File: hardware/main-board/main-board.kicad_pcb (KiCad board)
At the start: 2 copper layers, 180 x 55 mm, 95 parts, among them J1 BARREL_JACK, J2 CONN_01X10, J3 CONN_01X10, J4 USB_OTG, J5 CONN_02X05, J6 SMA, Q1 DDTD113ZC, Q2 DDTD113ZC, Q3 DDTD113ZC, Q4 DDTD113ZC, Q5 DDTD113ZC, Q6 FDB14N30TM, Q7 DDTD113ZC, Q8 DDTD113ZC, Q9 DDTD113ZC, SW1 SW_Push, SW2 SW_Push, SW3 SW_Push, SW4 SW_Push, U1 LD1117S33TR, U2 MAX1771, U3 STM32F302C, U4 FGPMMOPA6H, Y1 8MHz, Y2 32.768kHz

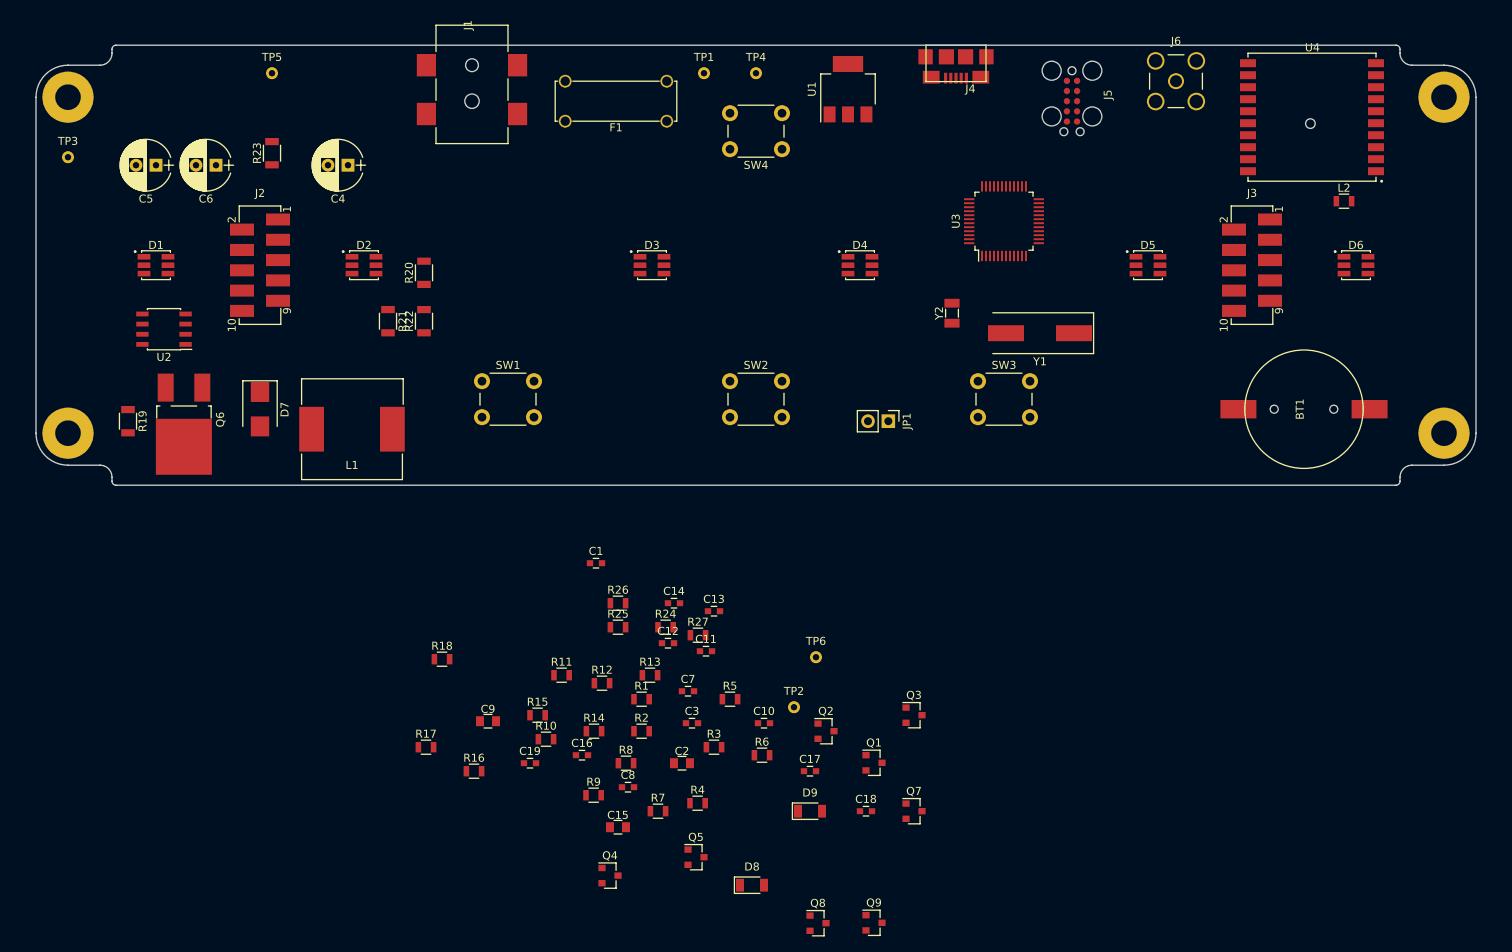
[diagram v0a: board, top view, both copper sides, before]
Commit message: Working on main board layout
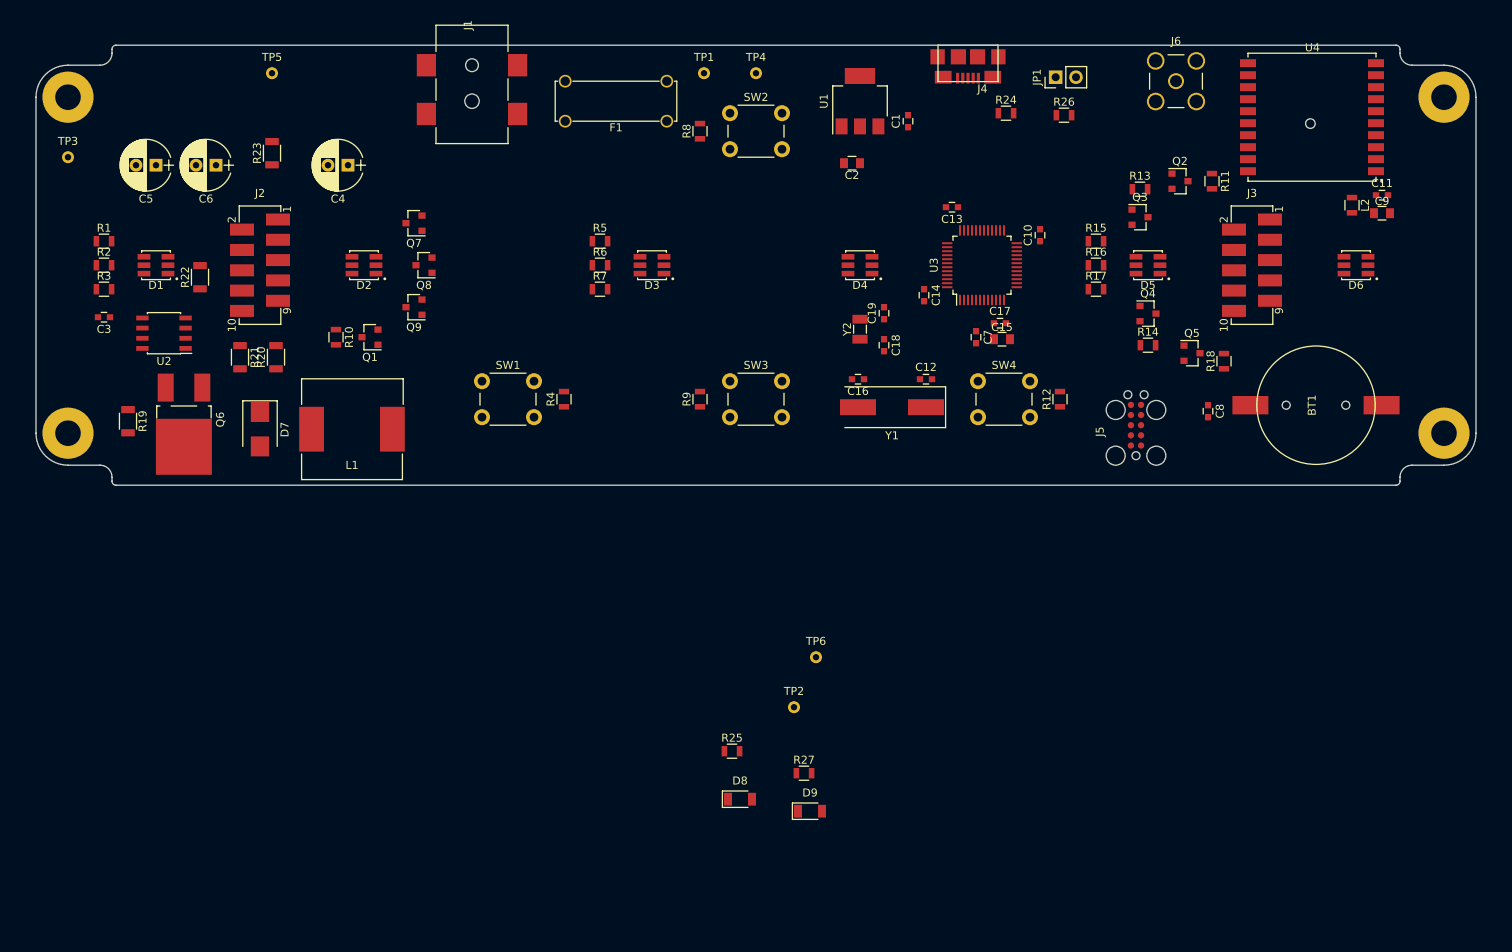
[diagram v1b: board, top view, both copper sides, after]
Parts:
- moved C9 128.5 mm to (228.2, 83.5)
- moved R18 104.6 mm to (208.5, 102.0), turned to 90 degrees
- moved R11 102.1 mm to (207.0, 79.5), turned to 270 degrees
- moved C11 101.9 mm to (228.2, 81.2)
- moved R17 101.4 mm to (192.5, 93.0)
- moved R16 100.2 mm to (192.5, 90.0)
- moved Q4 97.3 mm to (199.0, 96.0)
- moved Q7 96.5 mm to (107.2, 84.8), turned to 180 degrees
- moved Q9 96.1 mm to (107.2, 95.2), turned to 180 degrees
- moved Q8 95.9 mm to (108.5, 90.0), turned to 180 degrees
- moved R3 95.4 mm to (68.5, 93.0)
- moved R15 91.6 mm to (192.5, 87.0)
- moved C3 89.3 mm to (68.5, 96.5), turned to 180 degrees
- moved R2 88.9 mm to (68.5, 90.0)
- moved Q5 88.4 mm to (204.5, 101.0)
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
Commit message: Working on main board layout
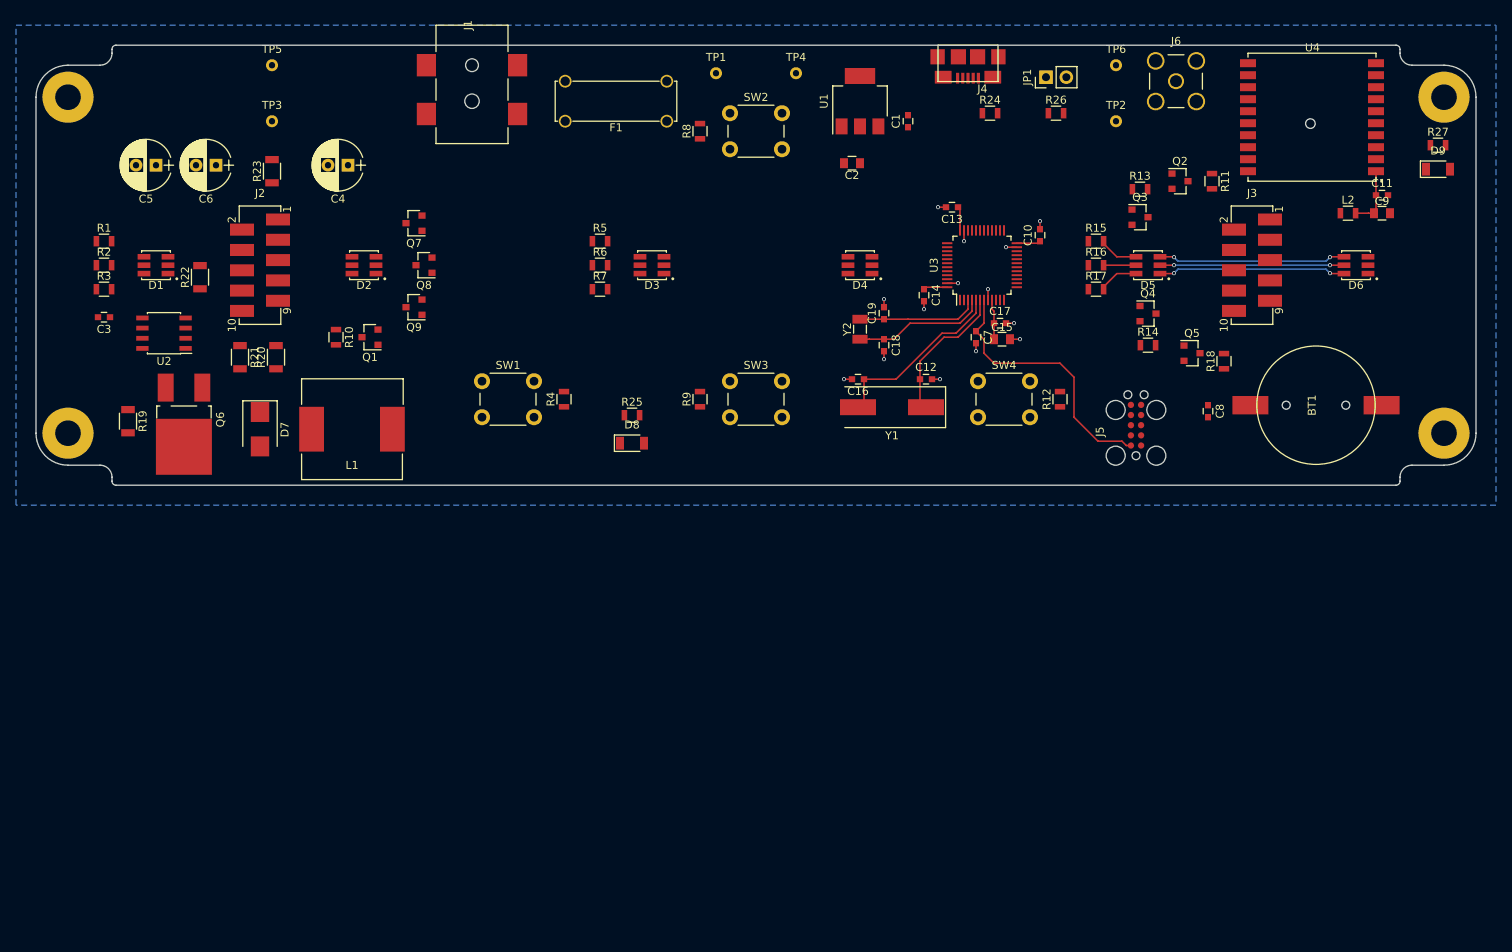
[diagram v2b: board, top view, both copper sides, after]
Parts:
- moved D9 112.3 mm to (235.2, 78.0)
- moved R27 111.5 mm to (235.2, 75.0)
- moved TP2 83.6 mm to (195.0, 72.0)
- moved TP6 83.0 mm to (195.0, 65.0)
- moved D8 46.5 mm to (134.5, 112.2)
- moved R25 43.8 mm to (134.5, 108.8)
- moved TP3 25.9 mm to (89.5, 72.0)
- moved TP4 5.00 mm to (155.0, 66.0)
- moved R23 2.25 mm to (89.5, 78.2)
- moved R24 2.00 mm to (179.2, 71.0)
- moved TP1 1.50 mm to (145.0, 66.0)
- moved JP1 1.21 mm to (186.2, 66.5)
- moved L2 1.12 mm to (224.0, 83.5), turned to 0 degrees
- moved R26 1.03 mm to (187.5, 71.0)
- moved TP5 1.00 mm to (89.5, 65.0)
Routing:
- net /NRST: track 0.00 -> 33.6 mm
- net Net-(D5-Pad3): track 0.00 -> 23.5 mm, vias 0 -> 2
- net Net-(D5-Pad1): track 0.00 -> 23.5 mm, vias 0 -> 2
- net Net-(D5-Pad2): track 0.00 -> 23.0 mm, vias 0 -> 2
- net Net-(C16-Pad1): track 0.00 -> 22.9 mm
- net Net-(C12-Pad1): track 0.00 -> 17.8 mm
- net Net-(C18-Pad1): track 0.00 -> 16.8 mm
- net GND: track 0.00 -> 15.6 mm, vias 0 -> 14
- net Net-(C19-Pad1): track 0.00 -> 15.2 mm
- net +3V3: track 0.00 -> 14.0 mm
- net Net-(C11-Pad1): track 0.00 -> 7.65 mm
- net Net-(D5-Pad6): track 0.00 -> 5.03 mm
- net Net-(D5-Pad4): track 0.00 -> 5.03 mm
- net Net-(D5-Pad5): track 0.00 -> 4.05 mm
- added copper zone on B.Cu, net GND
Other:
- net class Default: trace_width 0.25 -> 0.2; via_dia 0.6 -> 0.5; via_drill 0.4 -> 0.34
- rule pad_to_mask_clearance: 0.2 -> 0.05
- rule via_min_drill: 0.3 -> 0.34
- rule via_min_size: 0.4 -> 0.5

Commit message: Working on main board layout
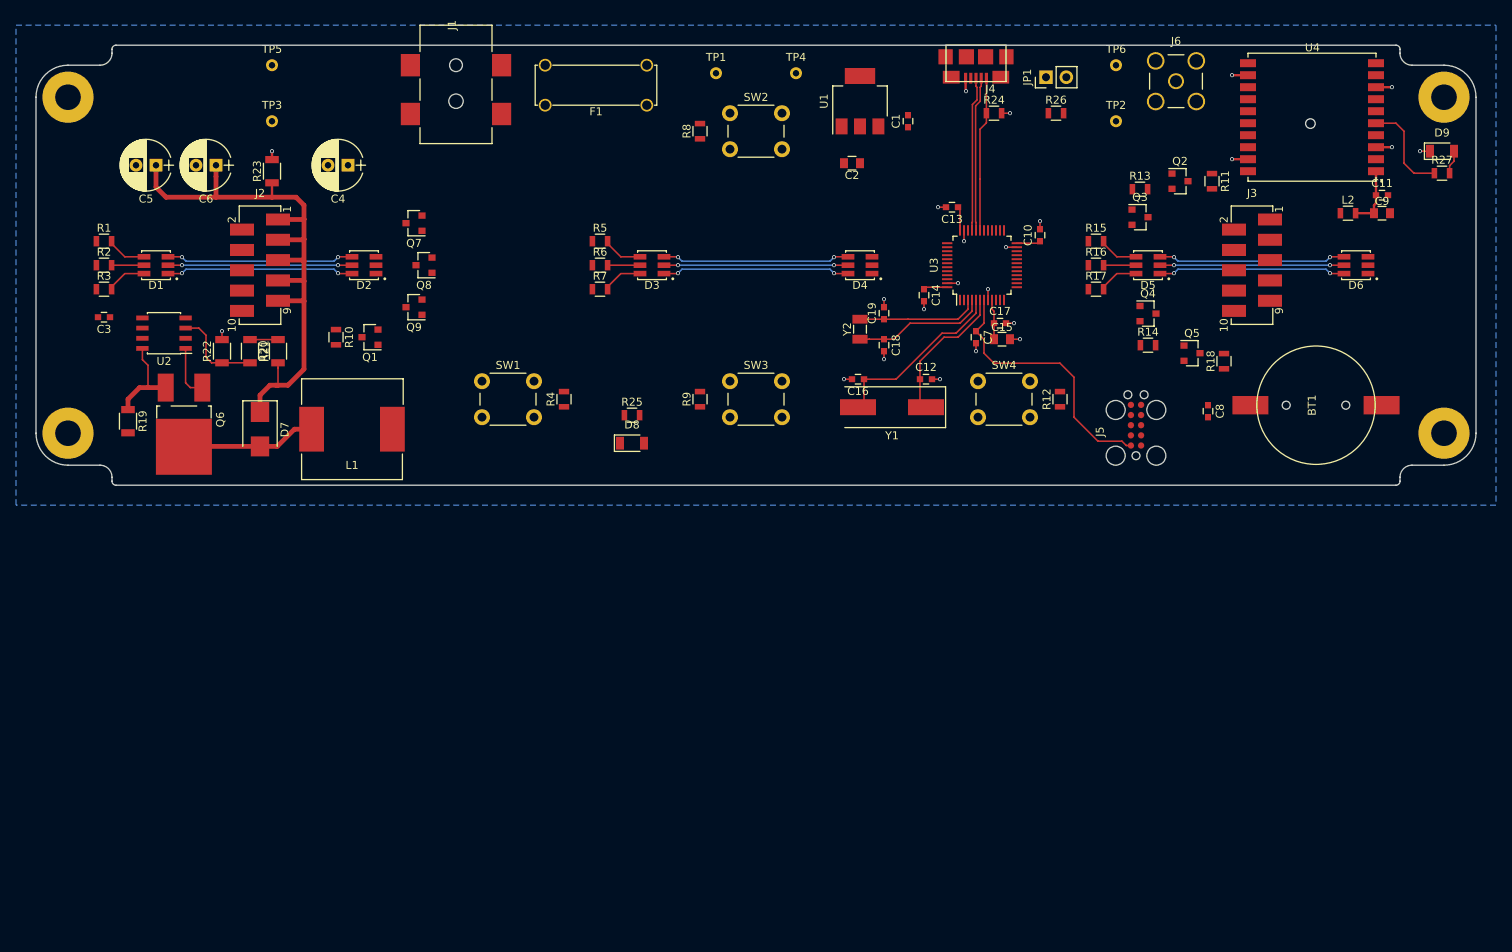
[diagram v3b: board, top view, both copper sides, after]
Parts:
- moved R22 9.65 mm to (83.2, 100.8)
- moved R27 3.54 mm to (235.8, 78.5)
- moved F1 3.20 mm to (130.0, 67.5)
- moved D9 2.30 mm to (235.8, 75.8)
- moved J1 2.00 mm to (112.5, 60.0)
- moved R21 1.46 mm to (86.8, 100.8)
- moved J4 1.00 mm to (177.5, 62.5)
- moved R20 0.79 mm to (90.2, 100.8)
- moved R24 0.50 mm to (179.8, 71.0)
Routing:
- net HT: track 0.00 -> 76.6 mm
- net Net-(D1-Pad3): track 0.00 -> 23.5 mm, vias 0 -> 2
- net Net-(D1-Pad1): track 0.00 -> 23.5 mm, vias 0 -> 2
- net Net-(D3-Pad3): track 0.00 -> 23.5 mm, vias 0 -> 2
- net Net-(D3-Pad1): track 0.00 -> 23.5 mm, vias 0 -> 2
- net Net-(D3-Pad2): track 0.00 -> 23.0 mm, vias 0 -> 2
- net Net-(D1-Pad2): track 0.00 -> 23.0 mm, vias 0 -> 2
- net /USB_VBUS: track 0.00 -> 19.4 mm
- net /USB_D-: track 0.00 -> 19.3 mm
- net /USB_D+: track 0.00 -> 19.3 mm
- net Net-(D7-Pad2): track 0.00 -> 16.9 mm
- net GND: track 15.6 -> 29.7 mm, vias 14 -> 23
- net Net-(R27-Pad1): track 0.00 -> 12.2 mm
- net Net-(Q6-Pad3): track 0.00 -> 11.8 mm
- net Net-(R21-Pad2): track 0.00 -> 11.5 mm
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
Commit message: Working on main board layout
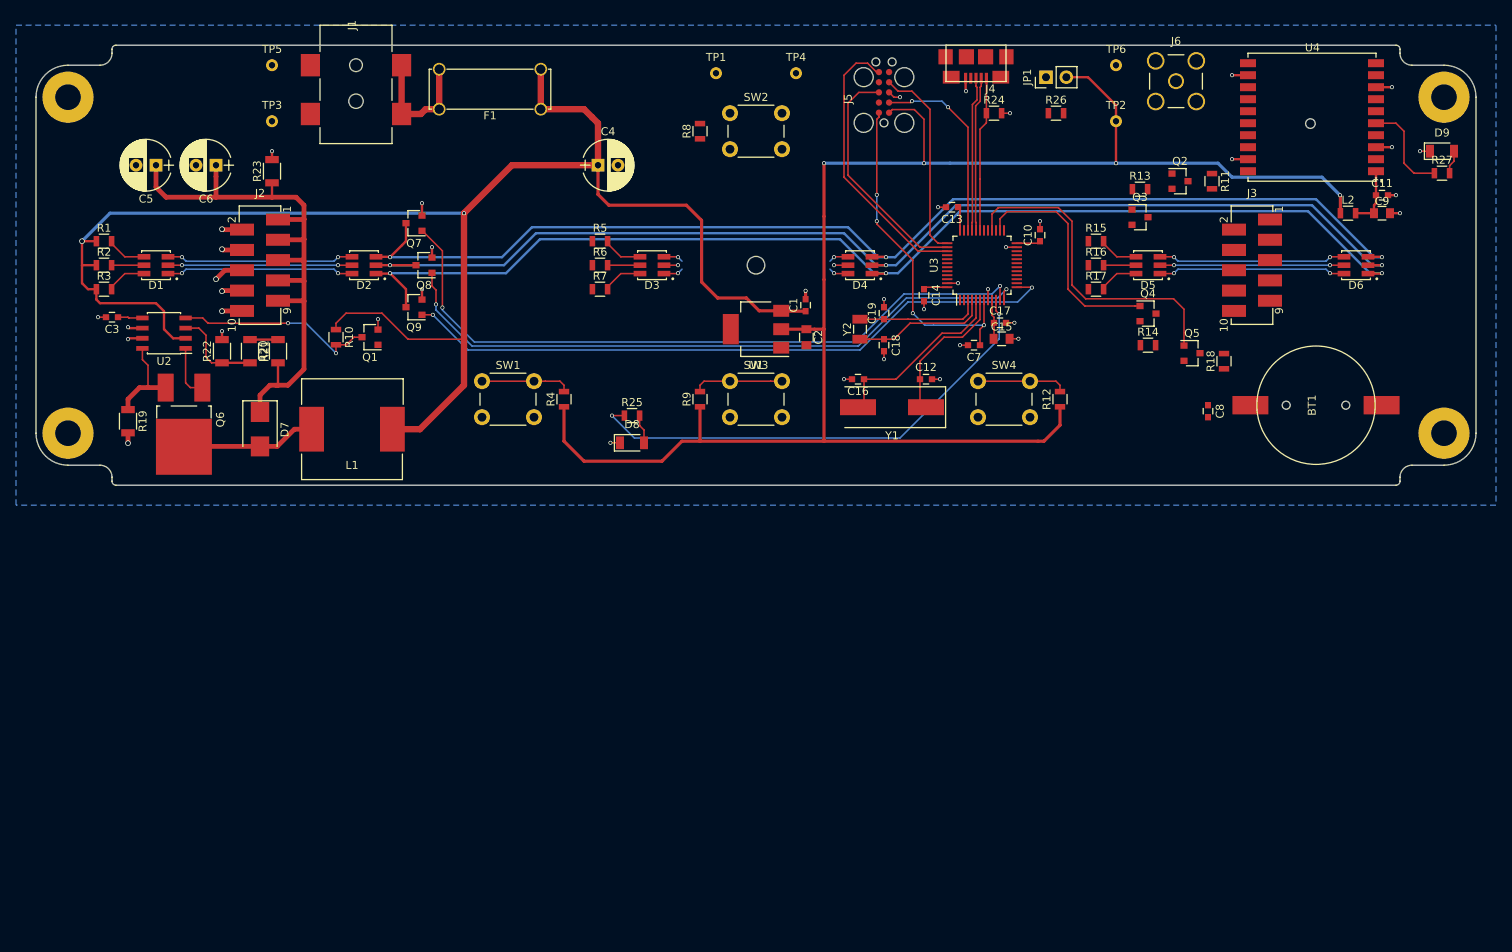
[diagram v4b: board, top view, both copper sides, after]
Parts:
- added REF**: MountingHole_2.2mm_M2, Mounting_Holes:MountingHole_2.2mm_M2, F.Cu at (150.0, 90.0)
- moved J5 52.2 mm to (166.0, 68.4)
- moved U1 31.3 mm to (150.0, 98.0), turned to 180 degrees
- moved C4 31.2 mm to (130.2, 77.5), turned to 0 degrees
- moved C1 26.3 mm to (156.2, 95.0)
- moved C2 22.5 mm to (156.3, 99.0), turned to 270 degrees
- moved F1 13.3 mm to (116.8, 68.0)
- moved J1 12.5 mm to (100.0, 60.0)
- moved C7 1.03 mm to (177.2, 100.0), turned to 180 degrees
- moved C3 1.00 mm to (69.5, 96.5)
- moved C15 0.07 mm to (180.7, 99.2)
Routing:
- net +3V3: track 14.0 -> 223.7 mm, vias 0 -> 4
- net +12V: track 0.00 -> 205.3 mm, vias 0 -> 2
- net Net-(D2-Pad1): track 0.00 -> 144.3 mm, vias 0 -> 3
- net Net-(D2-Pad3): track 0.00 -> 143.5 mm, vias 0 -> 3
- net Net-(D2-Pad2): track 0.00 -> 142.0 mm, vias 0 -> 3
- net /LED_RED: track 0.00 -> 87.0 mm, vias 0 -> 2
- net /LED_BLU: track 0.00 -> 83.2 mm, vias 0 -> 2
- net /LED_GRN: track 0.00 -> 82.4 mm, vias 0 -> 2
- net /DGB_LED: track 0.00 -> 61.3 mm, vias 0 -> 2
- net /DISP_DATA: track 0.00 -> 40.9 mm
- net /SWO/JTDO: track 0.00 -> 34.9 mm
- net GND: track 29.7 -> 59.6 mm, vias 23 -> 40
- net /JTDI: track 0.00 -> 29.6 mm
- net /DISP_CLK: track 0.00 -> 29.0 mm
- net Net-(Q1-Pad3): track 0.00 -> 25.3 mm, vias 0 -> 2
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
